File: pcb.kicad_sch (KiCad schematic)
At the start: 62 parts, among them J2 Conn_ARM_JTAG_SWD_10, P1 USB_C_Plug, Q1 CJE3139K, Q2 CJE3139K, Q5 2N7002, Q6 2N7002, SW1 SW_Push, U1 WE-TVS-82400102, U3 STM32F103C8T6, U6 74LVC2T45DC, U7 74LVC2T45DC, U8 74LVC2T45DC, U9 AP2112K-3.3, Y1 8MHz

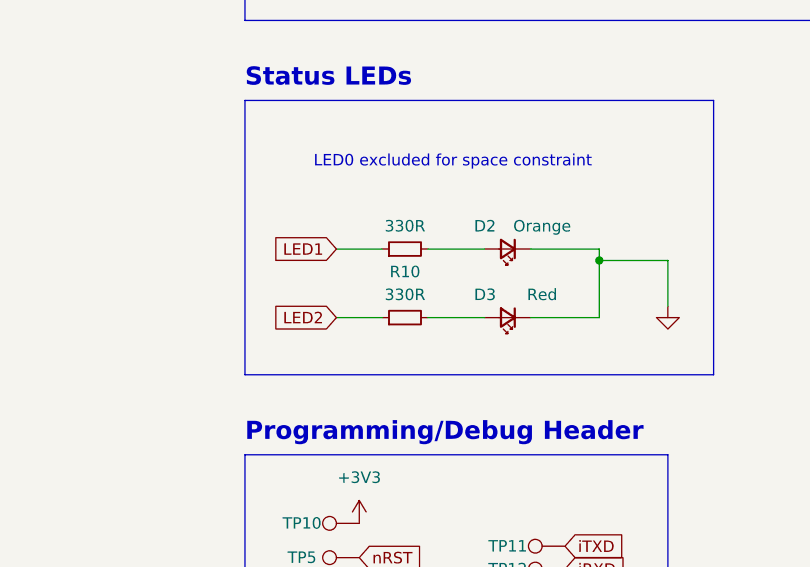
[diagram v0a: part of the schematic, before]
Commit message: dim leds
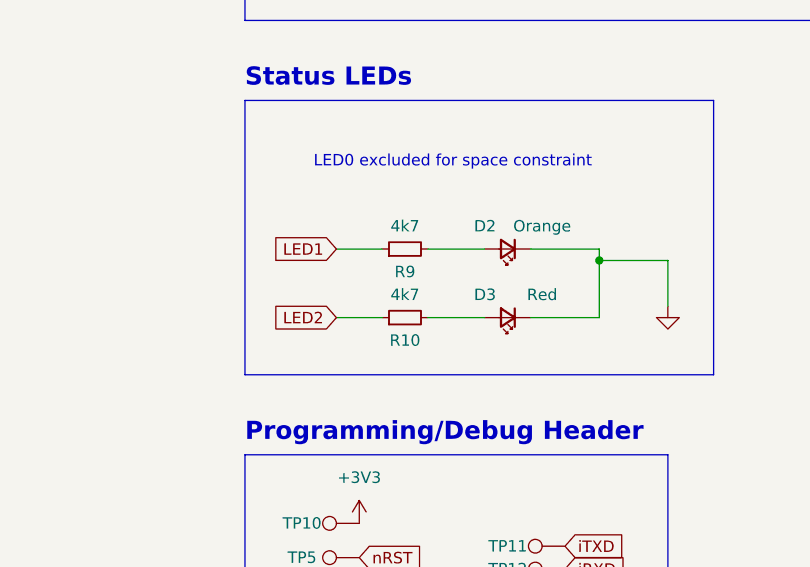
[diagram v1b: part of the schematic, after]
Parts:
- R10, R9: value 330R -> 4k7; LCSC C25104 -> C163826
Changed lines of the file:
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@@
   )
   (symbol (lib_id "Device:R_Small") (at 227.33 200.66 90) (unit 1)
-    (in_bom yes) (on_board yes) (dnp no) (fields_autoplaced)
-    (property "Reference" "R9" (at 227.33 195.58 90)
-      (effects (font (size 1.27 1.27)) hide)
-    )
-    (property "Value" "330R" (at 227.33 198.12 90)
+    (in_bom yes) (on_board yes) (dnp no)
+    (property "Reference" "R9" (at 227.33 203.2 90)
+      (effects (font (size 1.27 1.27)))
+    )
+    (property "Value" "4k7" (at 227.33 198.12 90)
       (effects (font (size 1.27 1.27)))
     )
@@
       (effects (font (size 1.27 1.27)) hide)
     )
-    (property "LCSC" "C25104" (at 227.33 200.66 0)
+    (property "LCSC" "C163826" (at 227.33 200.66 0)
       (effects (font (size 1.27 1.27)) hide)
     )
@@
   )
   (symbol (lib_id "Device:R_Small") (at 227.33 208.28 90) (unit 1)
-    (in_bom yes) (on_board yes) (dnp no) (fields_autoplaced)
-    (property "Reference" "R10" (at 227.33 203.2 90)
-      (effects (font (size 1.27 1.27)))
-    )
-    (property "Value" "330R" (at 227.33 205.74 90)
+    (in_bom yes) (on_board yes) (dnp no)
+    (property "Reference" "R10" (at 227.33 210.82 90)
+      (effects (font (size 1.27 1.27)))
+    )
+    (property "Value" "4k7" (at 227.33 205.74 90)
       (effects (font (size 1.27 1.27)))
     )
@@
       (effects (font (size 1.27 1.27)) hide)
     )
-    (property "LCSC" "C25104" (at 227.33 208.28 0)
-      (effects (font (size 1.27 1.27)) hide)
-    )
+    (property "LCSC" "C163826" (at 227.33 208.28 0)
+      (effects (font (size 1.27 1.27)) hide)
+    )
